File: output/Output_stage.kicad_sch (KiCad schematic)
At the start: 8 parts, among them J1 Conn_01x03_Socket, J2 Conn_01x02_Socket, J3 Conn_01x02_Socket, Q1 BTA41-600B, U1 MOC3041M

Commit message: Some tuning
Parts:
- J2, J3: value Conn_01x02_Socket -> Control/LED
- Q1: value BTA41-600B -> BTA41
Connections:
- net S/LINE: now reaches J1.3 (Pin_3), Q1.1 (A1), R2.1
- net LINE: now reaches J1.1 (Pin_1), Q1.2 (A2), R3.2
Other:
- note added: "Notes: 1. If the control signal comes from a 5V supply, R1 should be increased to 180 Ohms. 2. The power terminals at connector J1 can be interchanged."
- note removed: "Notes: 1. If the control signal comes from a 5V supply, R1 should be increased to 180 ohms. 2. The power terminals at connector CN 3 can be interchanged.."
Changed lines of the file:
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@@
     (date "2023-03-17")
   )
+  (junction (at 135.89 60.96) (diameter 0) (color 0 0 0 0)
+  )
   (junction (at 115.57 54.61) (diameter 0) (color 0 0 0 0)
   )
   (junction (at 135.89 44.45) (diameter 0) (color 0 0 0 0)
   )
-  (junction (at 135.89 60.96) (diameter 0) (color 0 0 0 0)
-  )
   (junction (at 81.28 34.29) (diameter 0) (color 0 0 0 0)
   )
   (junction (at 73.66 36.83) (diameter 0) (color 0 0 0 0)
   )
+  (junction (at 152.4 60.96) (diameter 0) (color 0 0 0 0)
+  )
+  (junction (at 152.4 44.45) (diameter 0) (color 0 0 0 0)
+  )
   (wire (pts (xy 81.28 25.4) (xy 81.28 34.29))
     (stroke (width 0) (type default))
@@
     (stroke (width 0) (type default))
   )
+  (wire (pts (xy 152.4 54.61) (xy 152.4 60.96))
+    (stroke (width 0) (type default))
+  )
+  (wire (pts (xy 73.66 40.64) (xy 73.66 36.83))
+    (stroke (width 0) (type default))
+  )
   (wire (pts (xy 124.46 60.96) (xy 135.89 60.96))
     (stroke (width 0) (type default))
   )
-  (wire (pts (xy 73.66 40.64) (xy 73.66 36.83))
-    (stroke (width 0) (type default))
-  )
-  (wire (pts (xy 152.4 54.61) (xy 152.4 60.96))
-    (stroke (width 0) (type default))
-  )
   (wire (pts (xy 152.4 44.45) (xy 135.89 44.45))
     (stroke (width 0) (type default))
@@
     (stroke (width 0) (type default))
   )
+  (wire (pts (xy 153.67 44.45) (xy 152.4 44.45))
+    (stroke (width 0) (type default))
+  )
   (wire (pts (xy 81.28 34.29) (xy 81.28 49.53))
     (stroke (width 0) (type default))
@@
     (stroke (width 0) (type default))
   )
+  (wire (pts (xy 153.67 60.96) (xy 152.4 60.96))
+    (stroke (width 0) (type default))
+  )
   (wire (pts (xy 113.03 54.61) (xy 115.57 54.61))
     (stroke (width 0) (type default))
   )
+  (wire (pts (xy 135.89 60.96) (xy 152.4 60.96))
+    (stroke (width 0) (type default))
+  )
   (wire (pts (xy 152.4 49.53) (xy 153.67 49.53))
     (stroke (width 0) (type default))
@@
     (stroke (width 0) (type default))
   )
-  (wire (pts (xy 135.89 60.96) (xy 135.89 57.15))
+  (wire (pts (xy 135.89 57.15) (xy 135.89 60.96))
     (stroke (width 0) (type default))
   )
@@
     (stroke (width 0) (type default))
   )
-  (wire (pts (xy 152.4 60.96) (xy 135.89 60.96))
-    (stroke (width 0) (type default))
-  )
   (wire (pts (xy 115.57 54.61) (xy 130.81 54.61))
     (stroke (width 0) (type default))
   )
-  (text "Notes:\n\n1. If the control signal comes from a 5V \nsupply, R1 should be increased to 180 ohms.\n\n2. The power terminals at connector CN 3 can \nbe interchanged.."
+  (text "Notes:\n\n1. If the control signal comes from a 5V \nsupply, R1 should be increased to 180 Ohms.\n\n2. The power terminals at connector J1 can \nbe interchanged."
     (at 101.6 34.29 0)
     (effects (font (size 1.27 1.27)) (justify left bottom))
   )
+  (symbol (lib_id "power:LINE") (at 153.67 44.45 270) (unit 1)
+    (in_bom yes) (on_board yes) (dnp no)
+    (property "Reference" "#PWR01" (at 149.86 44.45 0)
+      (effects (font (size 1.27 1.27)) hide)
+    )
+    (property "Value" "LINE" (at 156.21 44.45 90)
+      (effects (font (size 1.27 1.27)) (justify left))
+    )
+    (property "Footprint" "" (at 153.67 44.45 0)
+      (effects (font (size 1.27 1.27)) hide)
+    )
+    (property "Datasheet" "" (at 153.67 44.45 0)
+      (effects (font (size 1.27 1.27)) hide)
+    )
+    (pin "1")
+    (instances
+      (project "Output_stage"
+        (path "/47294ae8-0c3a-46fe-890e-b4eec645f7f7"
+          (reference "#PWR01") (unit 1)
+        )
+      )
+    )
+  )
+  (symbol (lib_name "LINE_1") (lib_id "power:LINE") (at 153.67 60.96 270) (unit 1)
+    (in_bom yes) (on_board yes) (dnp no)
+    (property "Reference" "#PWR02" (at 157.48 60.96 0)
+      (effects (font (size 1.27 1.27)) hide)
+    )
+    (property "Value" "S/LINE" (at 153.67 63.5 90)
+      (effects (font (size 1.27 1.27)) (justify left))
+    )
+    (property "Footprint" "" (at 153.67 60.96 0)
+      (effects (font (size 1.27 1.27)) hide)
+    )
+    (property "Datasheet" "" (at 153.67 60.96 0)
+      (effects (font (size 1.27 1.27)) hide)
+    )
+    (pin "1")
+    (instances
+      (project "Output_stage"
+        (path "/47294ae8-0c3a-46fe-890e-b4eec645f7f7"
+          (reference "#PWR02") (unit 1)
+        )
+      )
+    )
+  )
   (symbol (lib_id "Device:R") (at 120.65 60.96 270) (unit 1)
     (in_bom yes) (on_board yes) (dnp no) (fields_autoplaced)
@@
       (effects (font (size 1.27 1.27)))
     )
-    (property "Value" "Conn_01x02_Socket" (at 57.785 33.02 0)
+    (property "Value" "Control/LED" (at 57.785 33.02 0)
       (effects (font (size 1.27 1.27)))
     )
@@
       (effects (font (size 1.27 1.27)) (justify left))
     )
-    (property "Value" "BTA41-600B" (at 139.7 53.975 0)
+    (property "Value" "BTA41" (at 139.7 53.975 0)
       (effects (font (size 1.27 1.27)) (justify left))
     )
@@
       (effects (font (size 1.27 1.27)))
     )
-    (property "Value" "Conn_01x02_Socket" (at 57.785 24.13 0)
-      (effects (font (size 1.27 1.27)))
-    )
+    (property "Value" "Control/LED" (at 57.785 24.13 0)
+      (effects (font (size 1.27 1.27)))
+    )

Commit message: Update some symbols/footprints
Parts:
- R1, R2, R3: footprint Resistor_THT:R_Axial_DIN0207_L6.3mm_D2.5mm_P10.16mm_Horizontal -> PCM_Resistor_THT_AKL:R_Axial_DIN0207_L6.3mm_D2.5mm_P10.16mm_Horizontal
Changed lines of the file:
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@@
       (effects (font (size 1.27 1.27)))
     )
-    (property "Footprint" "Resistor_THT:R_Axial_DIN0207_L6.3mm_D2.5mm_P10.16mm_Horizontal" (at 120.65 59.182 90)
+    (property "Footprint" "PCM_Resistor_THT_AKL:R_Axial_DIN0207_L6.3mm_D2.5mm_P10.16mm_Horizontal" (at 120.65 59.182 90)
       (effects (font (size 1.27 1.27)) hide)
     )
@@
       (effects (font (size 1.27 1.27)))
     )
-    (property "Footprint" "Resistor_THT:R_Axial_DIN0207_L6.3mm_D2.5mm_P10.16mm_Horizontal" (at 120.65 46.228 90)
+    (property "Footprint" "PCM_Resistor_THT_AKL:R_Axial_DIN0207_L6.3mm_D2.5mm_P10.16mm_Horizontal" (at 120.65 46.228 90)
       (effects (font (size 1.27 1.27)) hide)
     )
@@
       (effects (font (size 1.27 1.27)) (justify left))
     )
-    (property "Footprint" "Resistor_THT:R_Axial_DIN0207_L6.3mm_D2.5mm_P10.16mm_Horizontal" (at 71.882 44.45 90)
+    (property "Footprint" "PCM_Resistor_THT_AKL:R_Axial_DIN0207_L6.3mm_D2.5mm_P10.16mm_Horizontal" (at 71.882 44.45 90)
       (effects (font (size 1.27 1.27)) hide)
     )

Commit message: Some update
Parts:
- Q1: footprint Package_TO_SOT_THT:TO-218-3_Vertical -> PCM_Package_TO_SOT_THT_AKL:TO-218-3_Vertical
- U1: footprint Package_DIP:DIP-6_W7.62mm_Socket_LongPads -> PCM_Package_DIP_AKL:DIP-6_W7.62mm_Socket_LongPads
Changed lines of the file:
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@@
   (title_block
     (title "Output stage for Mk2PVRouter")
-    (date "2023-03-17")
+    (date "2023-09-16")
+    (rev "2.0")
   )
   (junction (at 135.89 60.96) (diameter 0) (color 0 0 0 0)
@@
       (effects (font (size 1.27 1.27)) (justify left))
     )
-    (property "Footprint" "Package_TO_SOT_THT:TO-218-3_Vertical" (at 135.89 52.07 0)
+    (property "Footprint" "PCM_Package_TO_SOT_THT_AKL:TO-218-3_Vertical" (at 135.89 52.07 0)
       (effects (font (size 1.27 1.27)) hide)
     )
@@
       (effects (font (size 1.27 1.27)))
     )
-    (property "Footprint" "Package_DIP:DIP-6_W7.62mm_Socket_LongPads" (at 100.33 57.15 0)
+    (property "Footprint" "PCM_Package_DIP_AKL:DIP-6_W7.62mm_Socket_LongPads" (at 100.33 57.15 0)
       (effects (font (size 1.27 1.27) italic) (justify left) hide)
     )

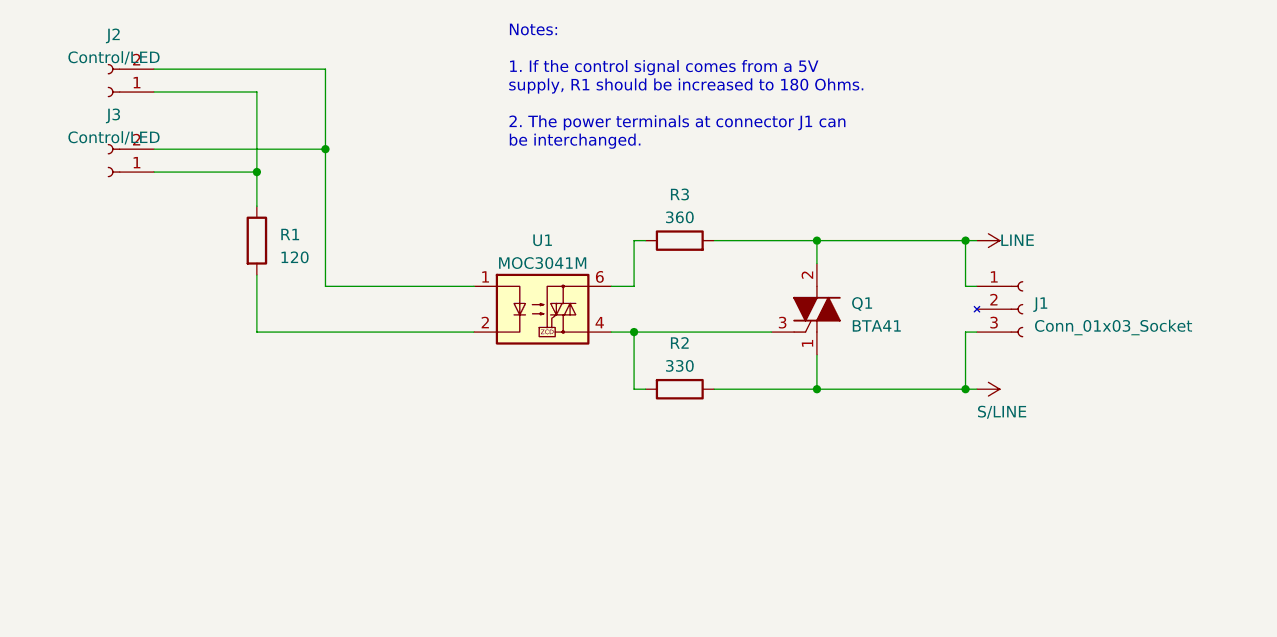
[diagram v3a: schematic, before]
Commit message: Update Output_stage.kicad_sch
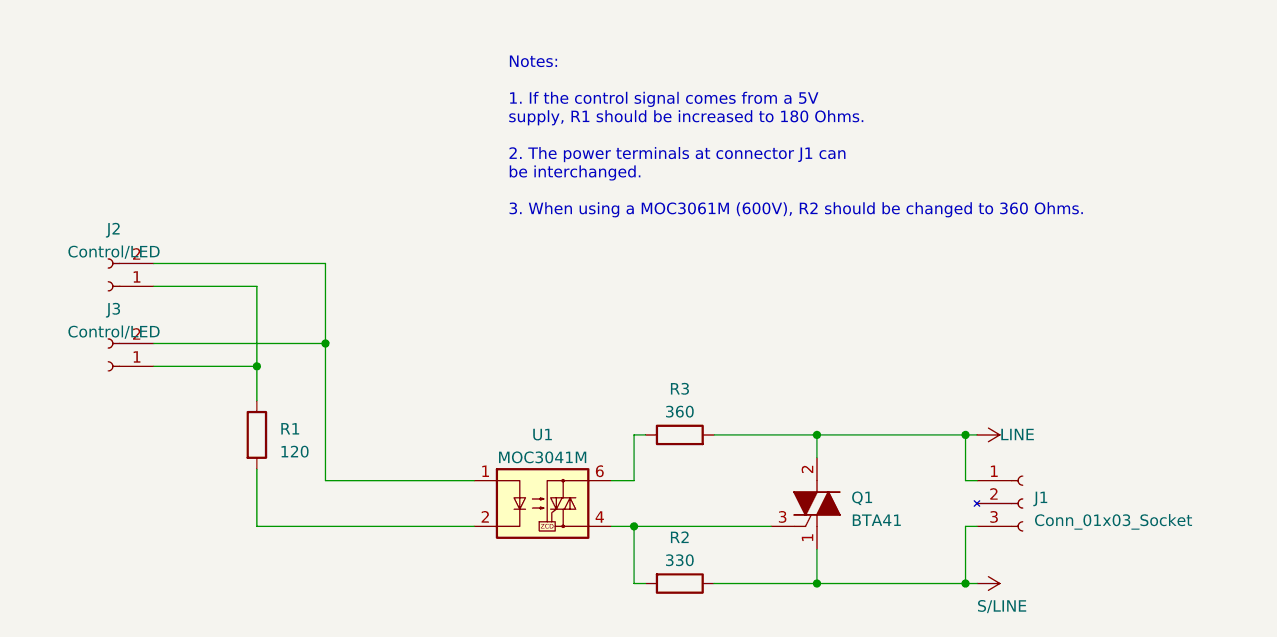
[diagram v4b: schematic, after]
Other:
- note added: "Notes: 1. If the control signal comes from a 5V supply, R1 should be increased to 180 Ohms. 2. The power terminals at connector J1 can be interchanged. 3. When using a MOC3061M (600V), R2 should be changed to 360 Ohms."
- note removed: "Notes: 1. If the control signal comes from a 5V supply, R1 should be increased to 180 Ohms. 2. The power terminals at connector J1 can be interchanged."
- moved on the sheet: J1, J2, J3, Q1, R1, R2, R3, U1
